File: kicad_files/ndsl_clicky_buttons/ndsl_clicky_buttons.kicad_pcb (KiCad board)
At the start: 2 copper layers, 28.1 x 23.1 mm, 13 parts, among them SW1 SW_Push, SW2 SW_Push, SW3 SW_Push, SW4 SW_Push

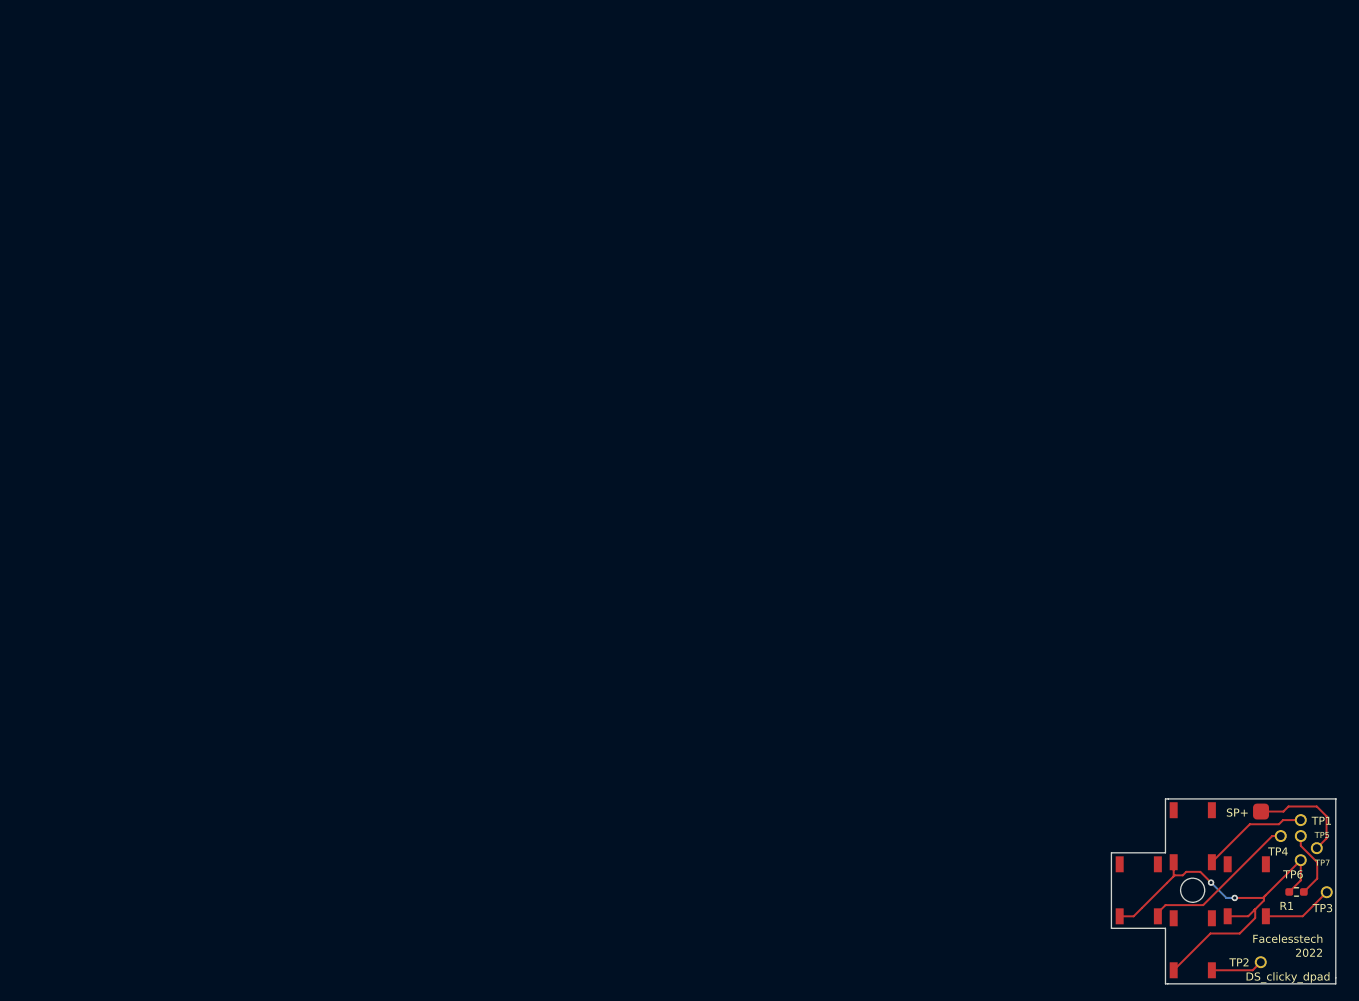
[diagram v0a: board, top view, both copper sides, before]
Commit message: Update d-pad PCB
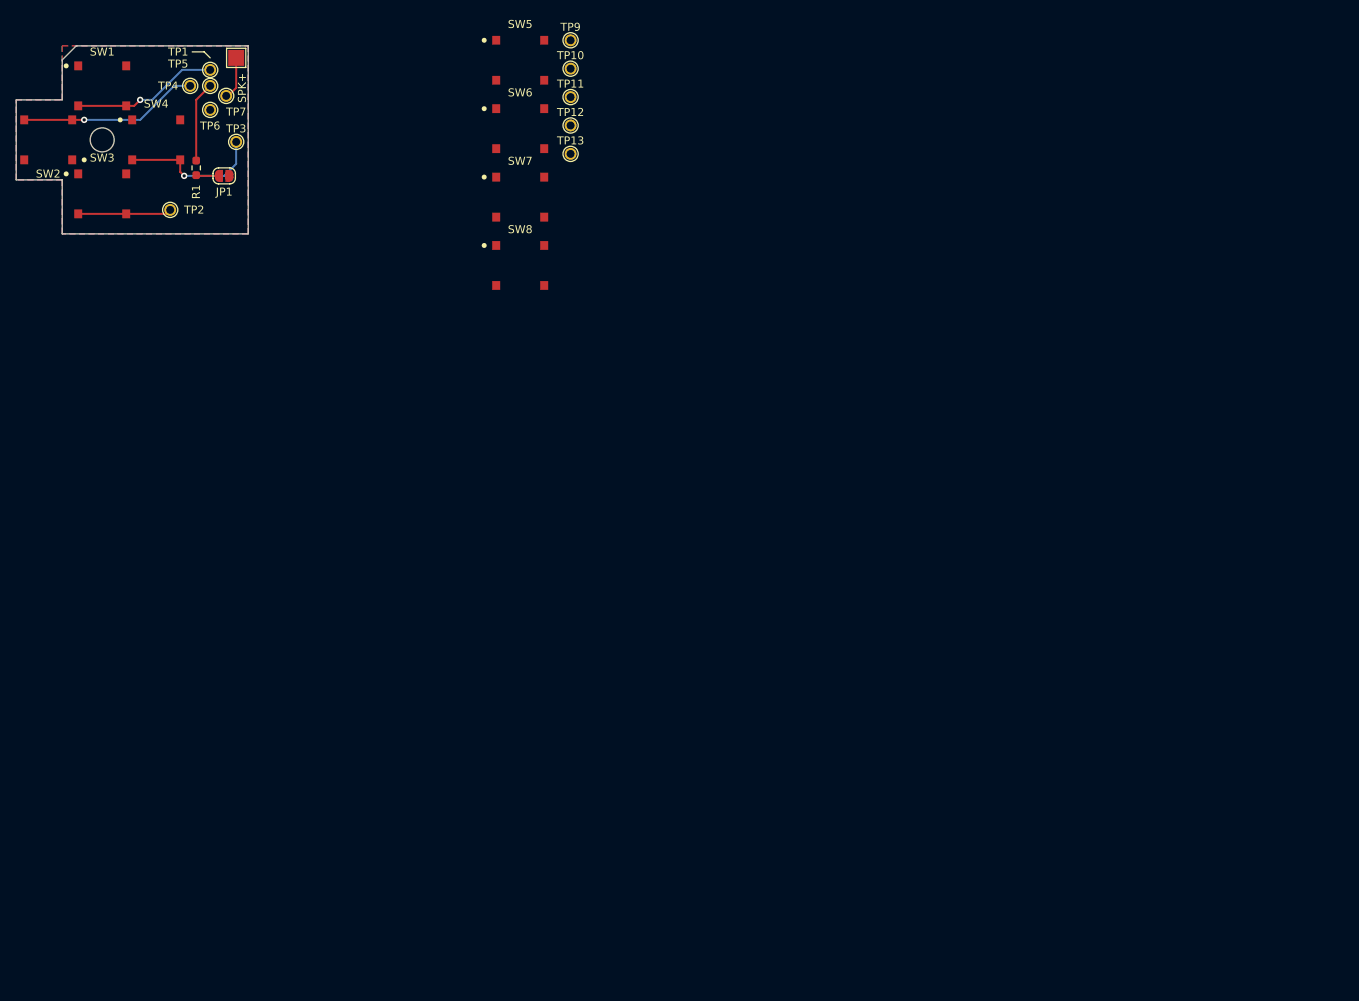
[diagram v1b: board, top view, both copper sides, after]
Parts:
- added JP1: SCREEN BYPASS, Jumper:SolderJumper-2_P1.3mm_Open_RoundedPad1.0x1.5mm, F.Cu at (22.0, 4.50)
- added SW5: X, ndsl_clicky_buttons:ALPS_SKRR, F.Cu at (59.0, -9.95)
- added SW6: Y, ndsl_clicky_buttons:ALPS_SKRR, F.Cu at (59.0, -1.40)
- added SW7: B, ndsl_clicky_buttons:ALPS_SKRR, F.Cu at (59.0, 7.15)
- added SW8: A, ndsl_clicky_buttons:ALPS_SKRR, F.Cu at (59.0, 15.7)
- added TP10: P00, ndsl_clicky_buttons:TestPoint_THTPad_D1.5mm_Drill1.0mm, F.Cu at (65.3, -8.90)
- added TP11: R01, ndsl_clicky_buttons:TestPoint_THTPad_D1.5mm_Drill1.0mm, F.Cu at (65.3, -5.35)
- added TP12: P01, ndsl_clicky_buttons:TestPoint_THTPad_D1.5mm_Drill1.0mm, F.Cu at (65.3, -1.80)
- added TP13: ABXY_GND, ndsl_clicky_buttons:TestPoint_THTPad_D1.5mm_Drill1.0mm, F.Cu at (65.3, 1.75)
- added TP9: R00, ndsl_clicky_buttons:TestPoint_THTPad_D1.5mm_Drill1.0mm, F.Cu at (65.3, -12.4)
- R1: value R -> 330
- SW1: value SW_Push -> UP; footprint buttons_custom:gba_sp_buttons -> ndsl_clicky_buttons:ALPS_SKRR
- SW2: value SW_Push -> LEFT; footprint buttons_custom:gba_sp_buttons -> ndsl_clicky_buttons:ALPS_SKRR
- SW3: value SW_Push -> DOWN; footprint buttons_custom:gba_sp_buttons -> ndsl_clicky_buttons:ALPS_SKRR
- SW4: value SW_Push -> RIGHT; footprint buttons_custom:gba_sp_buttons -> ndsl_clicky_buttons:ALPS_SKRR
- TP1: value TestPoint -> P06; footprint custom_connectors:1mm_test_point -> ndsl_clicky_buttons:TestPoint_THTPad_D1.5mm_Drill1.0mm
- TP2: value TestPoint -> P07; footprint custom_connectors:1mm_test_point -> ndsl_clicky_buttons:TestPoint_THTPad_D1.5mm_Drill1.0mm
- TP3: value TestPoint -> P04; footprint custom_connectors:1mm_test_point -> ndsl_clicky_buttons:TestPoint_THTPad_D1.5mm_Drill1.0mm
- TP4: value TestPoint -> P05; footprint custom_connectors:1mm_test_point -> ndsl_clicky_buttons:TestPoint_THTPad_D1.5mm_Drill1.0mm
- TP5: value TestPoint -> LEDA2; footprint custom_connectors:1mm_test_point -> ndsl_clicky_buttons:TestPoint_THTPad_D1.5mm_Drill1.0mm
- TP6: value TestPoint -> LEDC2; footprint custom_connectors:1mm_test_point -> ndsl_clicky_buttons:TestPoint_THTPad_D1.5mm_Drill1.0mm
- TP7: value TestPoint -> SPL0; footprint custom_connectors:1mm_test_point -> ndsl_clicky_buttons:TestPoint_THTPad_D1.5mm_Drill1.0mm
- TP8: renamed from SP+; value TestPoint -> SPK+; footprint custom_connectors:2mm_test_point_smd -> TestPoint:TestPoint_Pad_2.0x2.0mm
- moved TP7 165.6 mm to (22.2, -5.50)
- moved TP2 165.6 mm to (15.2, 8.75)
- moved SW2 165.5 mm to (0.00, 0.00), turned to 180 degrees
- moved TP3 165.5 mm to (23.5, 0.25)
- moved SW4 165.5 mm to (13.5, 0.00)
- moved SW3 165.5 mm to (6.75, 6.75)
- moved TP6 165.5 mm to (20.2, -3.75)
- moved TP1 165.5 mm to (20.2, -8.75)
- moved SW1 165.5 mm to (6.75, -6.75)
- moved TP5 165.5 mm to (20.2, -6.75)
- moved TP4 165.5 mm to (17.8, -6.75)
- moved R1 164.7 mm to (18.5, 3.50), turned to -90 degrees
- moved TP8 159.0 mm to (23.5, -10.2)
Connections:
- R1 pad 2: Net-(R1-Pad2) -> Net-(JP1-B)
- SW1 pad 1: Net-(R1-Pad2) -> DPAD_GND
- SW2 pad 1: Net-(R1-Pad2) -> DPAD_GND
- SW3 pad 1: Net-(R1-Pad2) -> DPAD_GND
- SW4 pad 1: Net-(R1-Pad2) -> DPAD_GND
- TP6 pad 1: Net-(R1-Pad2) -> DPAD_GND
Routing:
- net Net-(R1-Pad2): track 55.1 -> 0.00 mm, vias 2 -> 0
- net Net-(SW4-Pad2): track 8.86 -> 18.1 mm, vias 0 -> 1
- net Net-(TP7-Pad1): track 13.4 -> 5.52 mm
- net Net-(SW3-Pad2): track 6.53 -> 11.9 mm
- net Net-(SW1-Pad2): track 13.3 -> 18.4 mm, vias 0 -> 1
- net Net-(JP1-B): track 0.00 -> 2.89 mm
- net Net-(SW2-Pad2): track 19.8 -> 22.5 mm, vias 0 -> 1
- net Net-(R1-Pad1): track 8.53 -> 10.1 mm
- added copper zone on B.Cu, net DPAD_GND
- added copper zone on F.Cu, net DPAD_GND
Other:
- board size 28.1 x 23.1 mm -> 29 x 23.5 mm
- board text added: "nsdl_clicky_buttons"
- board text removed: "2022"
- board text removed: "DS_clicky_dpad"
- board text removed: "Facelesstech"

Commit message: Put both boards together
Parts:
- TP13: footprint ndsl_clicky_buttons:TestPoint_THTPad_D1.5mm_Drill1.0mm -> TestPoint:TestPoint_Pad_2.0x2.0mm
- moved TP11 35.7 mm to (31.5, 6.00)
- moved TP12 31.1 mm to (37.0, 11.0)
- moved TP9 30.2 mm to (35.3, -9.25)
- moved SW6 23.5 mm to (35.5, 0.00), turned to -90 degrees
- moved TP10 22.6 mm to (51.2, 8.75)
- moved SW8 17.9 mm to (50.5, 0.00), turned to 90 degrees
- moved TP13 17.7 mm to (52.0, -10.0)
- moved SW5 16.2 mm to (43.0, -7.50), turned to -90 degrees
- moved SW7 16.0 mm to (43.0, 7.50), turned to -90 degrees
- moved R1 3.48 mm to (19.8, 0.25)
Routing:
- net Net-(SW8-Pad2): track 0.00 -> 12.5 mm
- net Net-(SW5-Pad2): track 0.00 -> 11.8 mm
- net Net-(SW7-Pad2): track 0.00 -> 9.71 mm
- net Net-(SW6-Pad2): track 0.00 -> 9.62 mm
- net ABXY_GND: track 0.00 -> 3.85 mm, vias 0 -> 4
- net Net-(R1-Pad1): track 10.1 -> 7.54 mm
- net Net-(JP1-B): track 2.89 -> 4.00 mm
- added copper zone on B.Cu, net ABXY_GND
- added copper zone on F.Cu, net ABXY_GND
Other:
- board size 29 x 23.5 mm -> 58.2 x 24.5 mm
